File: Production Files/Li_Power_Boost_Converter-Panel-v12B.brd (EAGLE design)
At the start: 121.9 x 118.9 mm, 643 parts, among them U1 TPS61200, U10 TPS61200, U11 TPS61200, U12 TPS61200, U13 TPS61200, U14 TPS61200, U15 TPS61200, U16 TPS61200, U17 TPS61200, U18 TPS61200, U19 TPS61200, U2 TPS61200, U20 TPS61200, U21 TPS61200, U22 TPS61200, U23 TPS61200, U24 TPS61200, U25 TPS61200, U26 TPS61200, U27 TPS61200, U28 TPS61200, U29 TPS61200, U3 TPS61200, U30 TPS61200, U31 TPS61200, U32 TPS61200, U4 TPS61200, U5 TPS61200, U6 TPS61200, U7 TPS61200, U8 TPS61200, U9 TPS61200

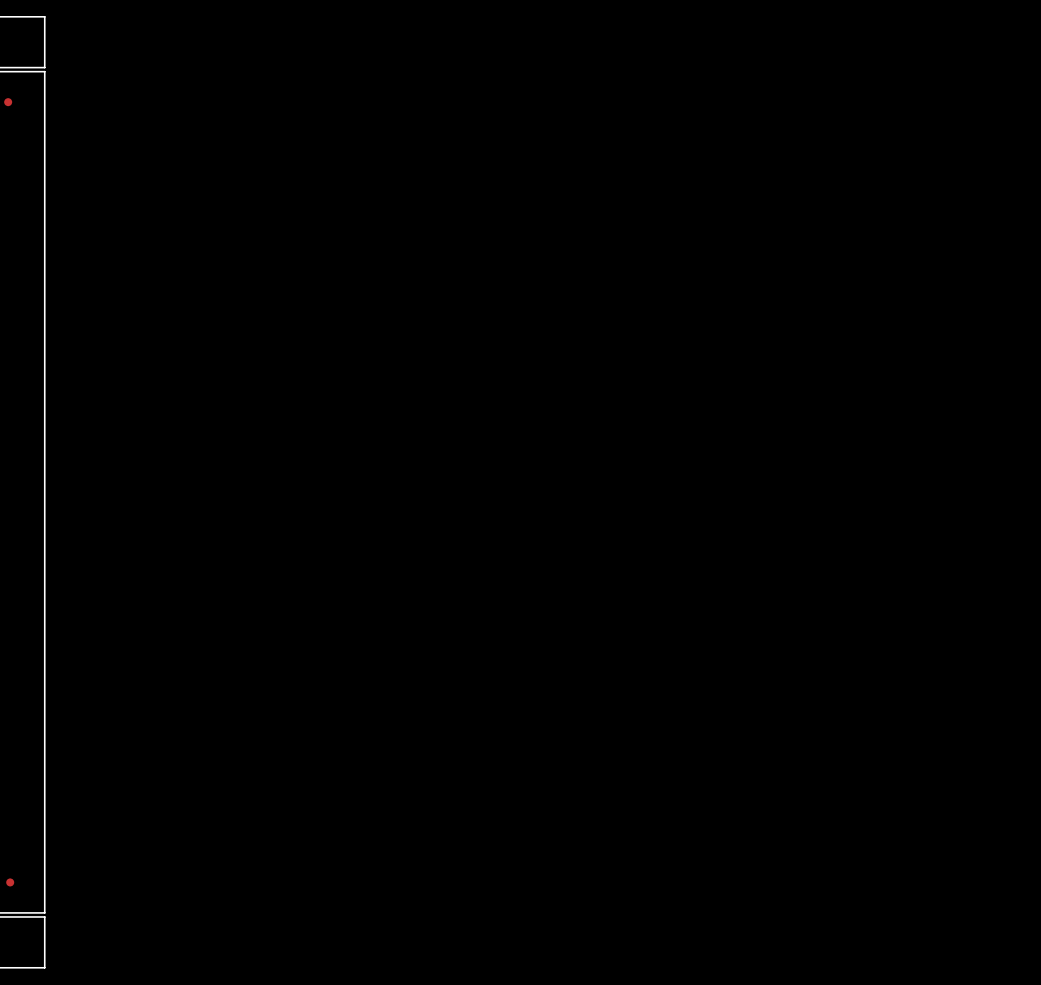
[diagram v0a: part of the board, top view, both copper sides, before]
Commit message: Repanel Production files
doubled panel size to optimize for foil use.
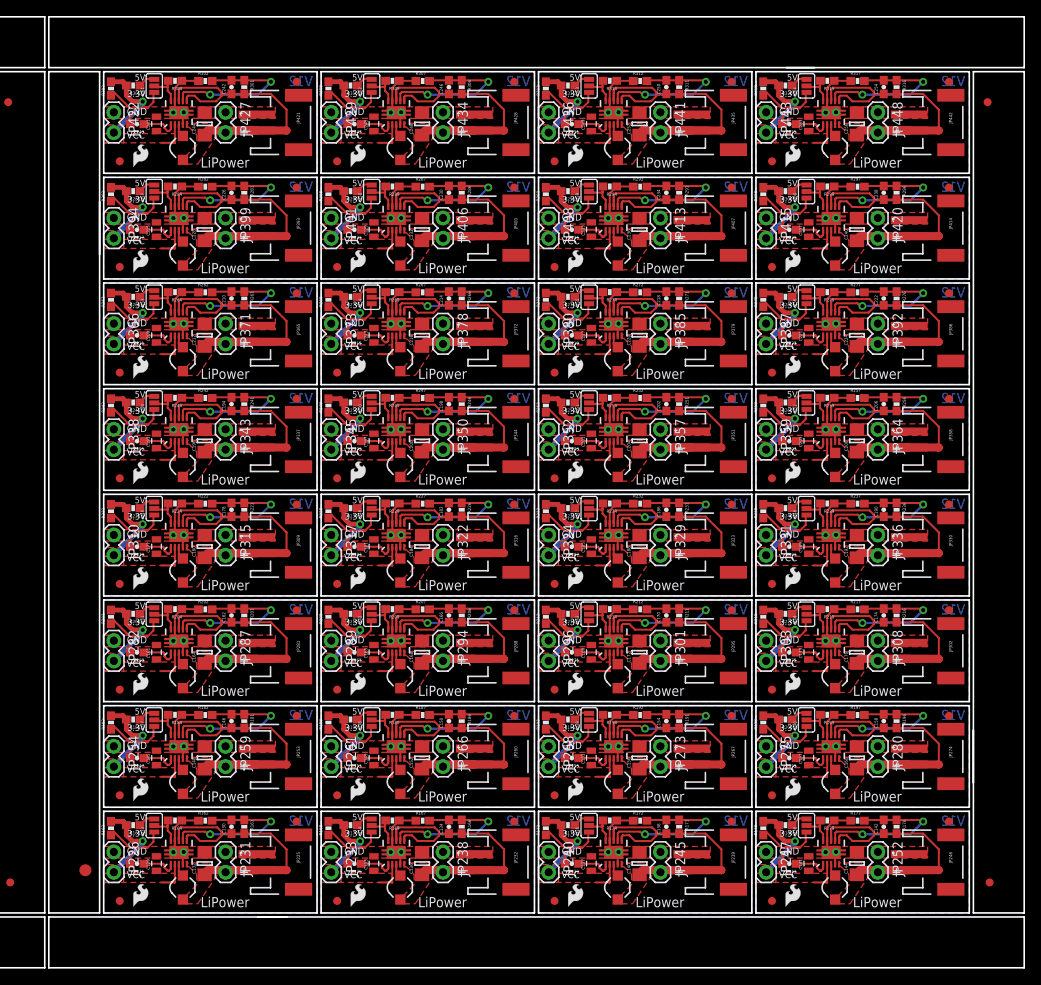
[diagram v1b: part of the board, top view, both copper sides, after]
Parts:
- added C129, C133, C137, C141, C145, C149, C153, C157, C161, C165, C169, C173, C177, C181, C185, C189, C193, C197, C201, C205, C209, C213, C217, C221, C225, C229, C233, C237, C241, C245, C249, C253: 22uF, CH_passive:0805
- added C130, C131, C134, C135, C138, C139, C142, C143, C146, C147, C150, C151, C154, C155, C158, C159, C162, C163, C166, C167, C170, C171, C174, C175, C178, C179, C182, C183, C186, C187, C190, C191, C194, C195, C198, C199, C202, C203, C206, C207, C210, C211, C214, C215, C218, C219, C222, C223, C226, C227, C230, C231, C234, C235, C238, C239, C242, C243, C246, C247, C250, C251, C254, C255: 0.1uF, SparkFun:0603-CAP
- added C132, C136, C140, C144, C148, C152, C156, C160, C164, C168, C172, C176, C180, C184, C188, C192, C196, C200, C204, C208, C212, C216, C220, C224, C228, C232, C236, C240, C244, C248, C252, C256: 10uF, CH_passive:1206
- added E$2, E$3: (no value), SparkFun-Aesthetics:FIDUCIAL-1X2
- added E$6: (no value), SparkFun-Aesthetics:FIDUCIAL-1.5X3
- added JP225, JP232, JP239, JP246, JP253, JP260, JP267, JP274, JP281, JP288, JP295, JP302, JP309, JP316, JP323, JP330, JP337, JP344, JP351, JP358, JP365, JP372, JP379, JP386, JP393, JP400, JP407, JP414, JP421, JP428, JP435, JP442: JST, SparkFun:JST-2-SMD
- added JP226, JP233, JP240, JP247, JP254, JP261, JP268, JP275, JP282, JP289, JP296, JP303, JP310, JP317, JP324, JP331, JP338, JP345, JP352, JP359, JP366, JP373, JP380, JP387, JP394, JP401, JP408, JP415, JP422, JP429, JP436, JP443: VOUT, SparkFun:1X02
- added JP227, JP234, JP241, JP248, JP255, JP262, JP269, JP276, JP283, JP290, JP297, JP304, JP311, JP318, JP325, JP332, JP339, JP346, JP353, JP360, JP367, JP374, JP381, JP388, JP395, JP402, JP409, JP416, JP423, JP430, JP437, JP444: LOGO-SFESK, SparkFun:SFE-LOGO-FLAME
- added JP228, JP229, JP235, JP236, JP242, JP243, JP249, JP250, JP256, JP257, JP263, JP264, JP270, JP271, JP277, JP278, JP284, JP285, JP291, JP292, JP298, JP299, JP305, JP306, JP312, JP313, JP319, JP320, JP326, JP327, JP333, JP334, JP340, JP341, JP347, JP348, JP354, JP355, JP361, JP362, JP368, JP369, JP375, JP376, JP382, JP383, JP389, JP390, JP396, JP397, JP403, JP404, JP410, JP411, JP417, JP418, JP424, JP425, JP431, JP432, JP438, JP439, JP445, JP446: FIDUCIAL1X2, SparkFun:FIDUCIAL-1X2
- added JP230, JP237, JP244, JP251, JP258, JP265, JP272, JP279, JP286, JP293, JP300, JP307, JP314, JP321, JP328, JP335, JP342, JP349, JP356, JP363, JP370, JP377, JP384, JP391, JP398, JP405, JP412, JP419, JP426, JP433, JP440, JP447: LOGO-SFENEW, SparkFun:SFE-NEW-WEBLOGO
- added JP231, JP238, JP245, JP252, JP259, JP266, JP273, JP280, JP287, JP294, JP301, JP308, JP315, JP322, JP329, JP336, JP343, JP350, JP357, JP364, JP371, JP378, JP385, JP392, JP399, JP406, JP413, JP420, JP427, JP434, JP441, JP448: VIN, SparkFun:1X02
- added L33, L34, L35, L36, L37, L38, L39, L40, L41, L42, L43, L44, L45, L46, L47, L48, L49, L50, L51, L52, L53, L54, L55, L56, L57, L58, L59, L60, L61, L62, L63, L64: 4.7uH, 1.2A, SparkFun:CDRH2D09
- added R161, R165, R166, R170, R171, R175, R176, R180, R181, R185, R186, R190, R191, R195, R196, R200, R201, R205, R206, R210, R211, R215, R216, R220, R221, R225, R226, R230, R231, R235, R236, R240, R241, R245, R246, R250, R251, R255, R256, R260, R261, R265, R266, R270, R271, R275, R276, R280, R281, R285, R286, R290, R291, R295, R296, R300, R301, R305, R306, R310, R311, R315, R316, R320: 2M, SparkFun:0603-RES
- added R162, R164, R167, R169, R172, R174, R177, R179, R182, R184, R187, R189, R192, R194, R197, R199, R202, R204, R207, R209, R212, R214, R217, R219, R222, R224, R227, R229, R232, R234, R237, R239, R242, R244, R247, R249, R252, R254, R257, R259, R262, R264, R267, R269, R272, R274, R277, R279, R282, R284, R287, R289, R292, R294, R297, R299, R302, R304, R307, R309, R312, R314, R317, R319: 220k, SparkFun:0603-RES
- added R163, R168, R173, R178, R183, R188, R193, R198, R203, R208, R213, R218, R223, R228, R233, R238, R243, R248, R253, R258, R263, R268, R273, R278, R283, R288, R293, R298, R303, R308, R313, R318: 1.2M, SparkFun:0603-RES
- added SJ33, SJ34, SJ35, SJ36, SJ37, SJ38, SJ39, SJ40, SJ41, SJ42, SJ43, SJ44, SJ45, SJ46, SJ47, SJ48, SJ49, SJ50, SJ51, SJ52, SJ53, SJ54, SJ55, SJ56, SJ57, SJ58, SJ59, SJ60, SJ61, SJ62, SJ63, SJ64: (no value), SparkFun:SJ_3_PASTE2&3
- added U$33, U$34, U$35, U$36, U$37, U$38, U$39, U$40, U$41, U$42, U$43, U$44, U$45, U$46, U$47, U$48, U$49, U$50, U$51, U$52, U$53, U$54, U$55, U$56, U$57, U$58, U$59, U$60, U$61, U$62, U$63, U$64: (no value), SparkFun-Aesthetics:OSHW-LOGO-S
- added U33, U34, U35, U36, U37, U38, U39, U40, U41, U42, U43, U44, U45, U46, U47, U48, U49, U50, U51, U52, U53, U54, U55, U56, U57, U58, U59, U60, U61, U62, U63, U64: TPS61200, SparkFun:QFN-10_PAD
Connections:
- new net 3.3V32: R163.1, SJ33.1
- new net 3.3V33: R168.1, SJ34.1
- new net 3.3V34: R173.1, SJ35.1
- new net 3.3V35: R178.1, SJ36.1
- new net 3.3V36: R183.1, SJ37.1
- new net 3.3V37: R188.1, SJ38.1
- new net 3.3V38: R193.1, SJ39.1
- new net 3.3V39: R198.1, SJ40.1
- new net 3.3V40: R203.1, SJ41.1
- new net 3.3V41: R208.1, SJ42.1
- new net 3.3V42: R213.1, SJ43.1
- new net 3.3V43: R218.1, SJ44.1
- new net 3.3V44: R223.1, SJ45.1
- new net 3.3V45: R228.1, SJ46.1
- new net 3.3V46: R233.1, SJ47.1
- new net 3.3V47: R238.1, SJ48.1
- new net 3.3V48: R243.1, SJ49.1
- new net 3.3V49: R248.1, SJ50.1
- new net 3.3V50: R253.1, SJ51.1
- new net 3.3V51: R258.1, SJ52.1
- new net 3.3V52: R263.1, SJ53.1
- new net 3.3V53: R268.1, SJ54.1
- new net 3.3V54: R273.1, SJ55.1
- new net 3.3V55: R278.1, SJ56.1
- new net 3.3V56: R283.1, SJ57.1
- new net 3.3V57: R288.1, SJ58.1
- new net 3.3V58: R293.1, SJ59.1
- new net 3.3V59: R298.1, SJ60.1
- new net 3.3V60: R303.1, SJ61.1
- new net 3.3V61: R308.1, SJ62.1
- new net 3.3V62: R313.1, SJ63.1
- new net 3.3V63: R318.1, SJ64.1
- new net 5V32: R165.1, SJ33.3
- new net 5V33: R170.1, SJ34.3
- new net 5V34: R175.1, SJ35.3
- new net 5V35: R180.1, SJ36.3
- new net 5V36: R185.1, SJ37.3
- new net 5V37: R190.1, SJ38.3
- new net 5V38: R195.1, SJ39.3
- new net 5V39: R200.1, SJ40.3
- new net 5V40: R205.1, SJ41.3
- new net 5V41: R210.1, SJ42.3
- new net 5V42: R215.1, SJ43.3
- new net 5V43: R220.1, SJ44.3
- new net 5V44: R225.1, SJ45.3
- new net 5V45: R230.1, SJ46.3
- new net 5V46: R235.1, SJ47.3
- new net 5V47: R240.1, SJ48.3
- new net 5V48: R245.1, SJ49.3
- new net 5V49: R250.1, SJ50.3
- new net 5V50: R255.1, SJ51.3
- new net 5V51: R260.1, SJ52.3
- new net 5V52: R265.1, SJ53.3
- new net 5V53: R270.1, SJ54.3
- new net 5V54: R275.1, SJ55.3
- new net 5V55: R280.1, SJ56.3
- new net 5V56: R285.1, SJ57.3
- new net 5V57: R290.1, SJ58.3
- new net 5V58: R295.1, SJ59.3
- new net 5V59: R300.1, SJ60.3
- new net 5V60: R305.1, SJ61.3
- new net 5V61: R310.1, SJ62.3
- new net 5V62: R315.1, SJ63.3
- new net 5V63: R320.1, SJ64.3
- new net FB32: R164.2, SJ33.2, U33.10
- new net FB33: R169.2, SJ34.2, U34.10
- new net FB34: R174.2, SJ35.2, U35.10
- new net FB35: R179.2, SJ36.2, U36.10
- new net FB36: R184.2, SJ37.2, U37.10
- new net FB37: R189.2, SJ38.2, U38.10
- new net FB38: R194.2, SJ39.2, U39.10
- new net FB39: R199.2, SJ40.2, U40.10
- new net FB40: R204.2, SJ41.2, U41.10
- new net FB41: R209.2, SJ42.2, U42.10
- new net FB42: R214.2, SJ43.2, U43.10
- new net FB43: R219.2, SJ44.2, U44.10
- new net FB44: R224.2, SJ45.2, U45.10
- new net FB45: R229.2, SJ46.2, U46.10
- new net FB46: R234.2, SJ47.2, U47.10
- new net FB47: R239.2, SJ48.2, U48.10
- new net FB48: R244.2, SJ49.2, U49.10
- new net FB49: R249.2, SJ50.2, U50.10
- new net FB50: R254.2, SJ51.2, U51.10
- new net FB51: R259.2, SJ52.2, U52.10
- new net FB52: R264.2, SJ53.2, U53.10
- new net FB53: R269.2, SJ54.2, U54.10
- new net FB54: R274.2, SJ55.2, U55.10
- new net FB55: R279.2, SJ56.2, U56.10
- new net FB56: R284.2, SJ57.2, U57.10
- new net FB57: R289.2, SJ58.2, U58.10
- new net FB58: R294.2, SJ59.2, U59.10
- new net FB59: R299.2, SJ60.2, U60.10
- new net FB60: R304.2, SJ61.2, U61.10
- new net FB61: R309.2, SJ62.2, U62.10
- new net FB62: R314.2, SJ63.2, U63.10
- new net FB63: R319.2, SJ64.2, U64.10
- new net GND32: C129.2, C131.2, C132.2, JP225.1, JP226.1, JP231.1, R162.1, R164.1, U33.11, U33.12, U33.13, U33.14, U33.15, U33.4, U33.9
- new net GND33: C133.2, C135.2, C136.2, JP232.1, JP233.1, JP238.1, R167.1, R169.1, U34.11, U34.12, U34.13, U34.14, U34.15, U34.4, U34.9
- new net GND34: C137.2, C139.2, C140.2, JP239.1, JP240.1, JP245.1, R172.1, R174.1, U35.11, U35.12, U35.13, U35.14, U35.15, U35.4, U35.9
- new net GND35: C141.2, C143.2, C144.2, JP246.1, JP247.1, JP252.1, R177.1, R179.1, U36.11, U36.12, U36.13, U36.14, U36.15, U36.4, U36.9
- new net GND36: C145.2, C147.2, C148.2, JP253.1, JP254.1, JP259.1, R182.1, R184.1, U37.11, U37.12, U37.13, U37.14, U37.15, U37.4, U37.9
- new net GND37: C149.2, C151.2, C152.2, JP260.1, JP261.1, JP266.1, R187.1, R189.1, U38.11, U38.12, U38.13, U38.14, U38.15, U38.4, U38.9
- new net GND38: C153.2, C155.2, C156.2, JP267.1, JP268.1, JP273.1, R192.1, R194.1, U39.11, U39.12, U39.13, U39.14, U39.15, U39.4, U39.9
- new net GND39: C157.2, C159.2, C160.2, JP274.1, JP275.1, JP280.1, R197.1, R199.1, U40.11, U40.12, U40.13, U40.14, U40.15, U40.4, U40.9
- new net GND40: C161.2, C163.2, C164.2, JP281.1, JP282.1, JP287.1, R202.1, R204.1, U41.11, U41.12, U41.13, U41.14, U41.15, U41.4, U41.9
- new net GND41: C165.2, C167.2, C168.2, JP288.1, JP289.1, JP294.1, R207.1, R209.1, U42.11, U42.12, U42.13, U42.14, U42.15, U42.4, U42.9
- new net GND42: C169.2, C171.2, C172.2, JP295.1, JP296.1, JP301.1, R212.1, R214.1, U43.11, U43.12, U43.13, U43.14, U43.15, U43.4, U43.9
- new net GND43: C173.2, C175.2, C176.2, JP302.1, JP303.1, JP308.1, R217.1, R219.1, U44.11, U44.12, U44.13, U44.14, U44.15, U44.4, U44.9
- new net GND44: C177.2, C179.2, C180.2, JP309.1, JP310.1, JP315.1, R222.1, R224.1, U45.11, U45.12, U45.13, U45.14, U45.15, U45.4, U45.9
- new net GND45: C181.2, C183.2, C184.2, JP316.1, JP317.1, JP322.1, R227.1, R229.1, U46.11, U46.12, U46.13, U46.14, U46.15, U46.4, U46.9
- new net GND46: C185.2, C187.2, C188.2, JP323.1, JP324.1, JP329.1, R232.1, R234.1, U47.11, U47.12, U47.13, U47.14, U47.15, U47.4, U47.9
- new net GND47: C189.2, C191.2, C192.2, JP330.1, JP331.1, JP336.1, R237.1, R239.1, U48.11, U48.12, U48.13, U48.14, U48.15, U48.4, U48.9
- new net GND48: C193.2, C195.2, C196.2, JP337.1, JP338.1, JP343.1, R242.1, R244.1, U49.11, U49.12, U49.13, U49.14, U49.15, U49.4, U49.9
- new net GND49: C197.2, C199.2, C200.2, JP344.1, JP345.1, JP350.1, R247.1, R249.1, U50.11, U50.12, U50.13, U50.14, U50.15, U50.4, U50.9
- new net GND50: C201.2, C203.2, C204.2, JP351.1, JP352.1, JP357.1, R252.1, R254.1, U51.11, U51.12, U51.13, U51.14, U51.15, U51.4, U51.9
- new net GND51: C205.2, C207.2, C208.2, JP358.1, JP359.1, JP364.1, R257.1, R259.1, U52.11, U52.12, U52.13, U52.14, U52.15, U52.4, U52.9
- new net GND52: C209.2, C211.2, C212.2, JP365.1, JP366.1, JP371.1, R262.1, R264.1, U53.11, U53.12, U53.13, U53.14, U53.15, U53.4, U53.9
- new net GND53: C213.2, C215.2, C216.2, JP372.1, JP373.1, JP378.1, R267.1, R269.1, U54.11, U54.12, U54.13, U54.14, U54.15, U54.4, U54.9
- new net GND54: C217.2, C219.2, C220.2, JP379.1, JP380.1, JP385.1, R272.1, R274.1, U55.11, U55.12, U55.13, U55.14, U55.15, U55.4, U55.9
- new net GND55: C221.2, C223.2, C224.2, JP386.1, JP387.1, JP392.1, R277.1, R279.1, U56.11, U56.12, U56.13, U56.14, U56.15, U56.4, U56.9
- new net GND56: C225.2, C227.2, C228.2, JP393.1, JP394.1, JP399.1, R282.1, R284.1, U57.11, U57.12, U57.13, U57.14, U57.15, U57.4, U57.9
- new net GND57: C229.2, C231.2, C232.2, JP400.1, JP401.1, JP406.1, R287.1, R289.1, U58.11, U58.12, U58.13, U58.14, U58.15, U58.4, U58.9
- new net GND58: C233.2, C235.2, C236.2, JP407.1, JP408.1, JP413.1, R292.1, R294.1, U59.11, U59.12, U59.13, U59.14, U59.15, U59.4, U59.9
- new net GND59: C237.2, C239.2, C240.2, JP414.1, JP415.1, JP420.1, R297.1, R299.1, U60.11, U60.12, U60.13, U60.14, U60.15, U60.4, U60.9
- new net GND60: C241.2, C243.2, C244.2, JP421.1, JP422.1, JP427.1, R302.1, R304.1, U61.11, U61.12, U61.13, U61.14, U61.15, U61.4, U61.9
- new net GND61: C245.2, C247.2, C248.2, JP428.1, JP429.1, JP434.1, R307.1, R309.1, U62.11, U62.12, U62.13, U62.14, U62.15, U62.4, U62.9
- new net GND62: C249.2, C251.2, C252.2, JP435.1, JP436.1, JP441.1, R312.1, R314.1, U63.11, U63.12, U63.13, U63.14, U63.15, U63.4, U63.9
- new net GND63: C253.2, C255.2, C256.2, JP442.1, JP443.1, JP448.1, R317.1, R319.1, U64.11, U64.12, U64.13, U64.14, U64.15, U64.4, U64.9
- new net N$100: C199.1, U50.1
- new net N$101: L51.P$1, U51.3
- new net N$102: C203.1, U51.1
- new net N$103: L52.P$1, U52.3
- new net N$104: C207.1, U52.1
- new net N$105: L53.P$1, U53.3
- new net N$106: C211.1, U53.1
- new net N$107: L54.P$1, U54.3
- new net N$108: C215.1, U54.1
- new net N$109: L55.P$1, U55.3
- new net N$110: C219.1, U55.1
- new net N$111: L56.P$1, U56.3
- new net N$112: C223.1, U56.1
- new net N$113: L57.P$1, U57.3
- new net N$114: C227.1, U57.1
- new net N$115: L58.P$1, U58.3
- new net N$116: C231.1, U58.1
- new net N$117: L59.P$1, U59.3
- new net N$118: C235.1, U59.1
- new net N$119: L60.P$1, U60.3
- new net N$120: C239.1, U60.1
- new net N$121: L61.P$1, U61.3
- new net N$122: C243.1, U61.1
- new net N$123: L62.P$1, U62.3
- new net N$124: C247.1, U62.1
- new net N$125: L63.P$1, U63.3
- new net N$126: C251.1, U63.1
- new net N$127: L64.P$1, U64.3
- new net N$128: C255.1, U64.1
- new net N$65: L33.P$1, U33.3
- new net N$66: C131.1, U33.1
- new net N$67: L34.P$1, U34.3
- new net N$68: C135.1, U34.1
- new net N$69: L35.P$1, U35.3
- new net N$70: C139.1, U35.1
- new net N$71: L36.P$1, U36.3
- new net N$72: C143.1, U36.1
- new net N$73: L37.P$1, U37.3
- new net N$74: C147.1, U37.1
- new net N$75: L38.P$1, U38.3
- new net N$76: C151.1, U38.1
- new net N$77: L39.P$1, U39.3
- new net N$78: C155.1, U39.1
- new net N$79: L40.P$1, U40.3
- new net N$80: C159.1, U40.1
- new net N$81: L41.P$1, U41.3
- new net N$82: C163.1, U41.1
- new net N$83: L42.P$1, U42.3
- new net N$84: C167.1, U42.1
- new net N$85: L43.P$1, U43.3
- new net N$86: C171.1, U43.1
- new net N$87: L44.P$1, U44.3
- new net N$88: C175.1, U44.1
- new net N$89: L45.P$1, U45.3
- new net N$90: C179.1, U45.1
- new net N$91: L46.P$1, U46.3
- new net N$92: C183.1, U46.1
- new net N$93: L47.P$1, U47.3
- new net N$94: C187.1, U47.1
- new net N$95: L48.P$1, U48.3
- new net N$96: C191.1, U48.1
- new net N$97: L49.P$1, U49.3
- new net N$98: C195.1, U49.1
- new net N$99: L50.P$1, U50.3
- new net UVLO32: C130.2, R161.1, R162.2, U33.7
- new net UVLO33: C134.2, R166.1, R167.2, U34.7
- new net UVLO34: C138.2, R171.1, R172.2, U35.7
- new net UVLO35: C142.2, R176.1, R177.2, U36.7
- new net UVLO36: C146.2, R181.1, R182.2, U37.7
- new net UVLO37: C150.2, R186.1, R187.2, U38.7
- new net UVLO38: C154.2, R191.1, R192.2, U39.7
- new net UVLO39: C158.2, R196.1, R197.2, U40.7
- new net UVLO40: C162.2, R201.1, R202.2, U41.7
- new net UVLO41: C166.2, R206.1, R207.2, U42.7
- new net UVLO42: C170.2, R211.1, R212.2, U43.7
- new net UVLO43: C174.2, R216.1, R217.2, U44.7
- new net UVLO44: C178.2, R221.1, R222.2, U45.7
- new net UVLO45: C182.2, R226.1, R227.2, U46.7
- new net UVLO46: C186.2, R231.1, R232.2, U47.7
- new net UVLO47: C190.2, R236.1, R237.2, U48.7
- new net UVLO48: C194.2, R241.1, R242.2, U49.7
- new net UVLO49: C198.2, R246.1, R247.2, U50.7
- new net UVLO50: C202.2, R251.1, R252.2, U51.7
- new net UVLO51: C206.2, R256.1, R257.2, U52.7
- new net UVLO52: C210.2, R261.1, R262.2, U53.7
- new net UVLO53: C214.2, R266.1, R267.2, U54.7
- new net UVLO54: C218.2, R271.1, R272.2, U55.7
- new net UVLO55: C222.2, R276.1, R277.2, U56.7
- new net UVLO56: C226.2, R281.1, R282.2, U57.7
- new net UVLO57: C230.2, R286.1, R287.2, U58.7
- new net UVLO58: C234.2, R291.1, R292.2, U59.7
- new net UVLO59: C238.2, R296.1, R297.2, U60.7
- new net UVLO60: C242.2, R301.1, R302.2, U61.7
- new net UVLO61: C246.2, R306.1, R307.2, U62.7
- new net UVLO62: C250.2, R311.1, R312.2, U63.7
- new net UVLO63: C254.2, R316.1, R317.2, U64.7
- new net VCC32: C129.1, JP226.2, R163.2, R165.2, U33.2
- new net VCC33: C133.1, JP233.2, R168.2, R170.2, U34.2
- new net VCC34: C137.1, JP240.2, R173.2, R175.2, U35.2
- new net VCC35: C141.1, JP247.2, R178.2, R180.2, U36.2
- new net VCC36: C145.1, JP254.2, R183.2, R185.2, U37.2
- new net VCC37: C149.1, JP261.2, R188.2, R190.2, U38.2
- new net VCC38: C153.1, JP268.2, R193.2, R195.2, U39.2
- new net VCC39: C157.1, JP275.2, R198.2, R200.2, U40.2
- new net VCC40: C161.1, JP282.2, R203.2, R205.2, U41.2
- new net VCC41: C165.1, JP289.2, R208.2, R210.2, U42.2
- new net VCC42: C169.1, JP296.2, R213.2, R215.2, U43.2
- new net VCC43: C173.1, JP303.2, R218.2, R220.2, U44.2
- new net VCC44: C177.1, JP310.2, R223.2, R225.2, U45.2
- new net VCC45: C181.1, JP317.2, R228.2, R230.2, U46.2
- new net VCC46: C185.1, JP324.2, R233.2, R235.2, U47.2
- new net VCC47: C189.1, JP331.2, R238.2, R240.2, U48.2
- new net VCC48: C193.1, JP338.2, R243.2, R245.2, U49.2
- new net VCC49: C197.1, JP345.2, R248.2, R250.2, U50.2
- new net VCC50: C201.1, JP352.2, R253.2, R255.2, U51.2
- new net VCC51: C205.1, JP359.2, R258.2, R260.2, U52.2
- new net VCC52: C209.1, JP366.2, R263.2, R265.2, U53.2
- new net VCC53: C213.1, JP373.2, R268.2, R270.2, U54.2
- new net VCC54: C217.1, JP380.2, R273.2, R275.2, U55.2
- new net VCC55: C221.1, JP387.2, R278.2, R280.2, U56.2
- new net VCC56: C225.1, JP394.2, R283.2, R285.2, U57.2
- new net VCC57: C229.1, JP401.2, R288.2, R290.2, U58.2
- new net VCC58: C233.1, JP408.2, R293.2, R295.2, U59.2
- new net VCC59: C237.1, JP415.2, R298.2, R300.2, U60.2
- new net VCC60: C241.1, JP422.2, R303.2, R305.2, U61.2
- new net VCC61: C245.1, JP429.2, R308.2, R310.2, U62.2
- new net VCC62: C249.1, JP436.2, R313.2, R315.2, U63.2
- new net VCC63: C253.1, JP443.2, R318.2, R320.2, U64.2
- new net VIN32: C130.1, C132.1, JP225.2, JP231.2, L33.P$2, R161.2, U33.5, U33.6, U33.8
- new net VIN33: C134.1, C136.1, JP232.2, JP238.2, L34.P$2, R166.2, U34.5, U34.6, U34.8
- new net VIN34: C138.1, C140.1, JP239.2, JP245.2, L35.P$2, R171.2, U35.5, U35.6, U35.8
- new net VIN35: C142.1, C144.1, JP246.2, JP252.2, L36.P$2, R176.2, U36.5, U36.6, U36.8
- new net VIN36: C146.1, C148.1, JP253.2, JP259.2, L37.P$2, R181.2, U37.5, U37.6, U37.8
- new net VIN37: C150.1, C152.1, JP260.2, JP266.2, L38.P$2, R186.2, U38.5, U38.6, U38.8
- new net VIN38: C154.1, C156.1, JP267.2, JP273.2, L39.P$2, R191.2, U39.5, U39.6, U39.8
- new net VIN39: C158.1, C160.1, JP274.2, JP280.2, L40.P$2, R196.2, U40.5, U40.6, U40.8
- new net VIN40: C162.1, C164.1, JP281.2, JP287.2, L41.P$2, R201.2, U41.5, U41.6, U41.8
- new net VIN41: C166.1, C168.1, JP288.2, JP294.2, L42.P$2, R206.2, U42.5, U42.6, U42.8
- new net VIN42: C170.1, C172.1, JP295.2, JP301.2, L43.P$2, R211.2, U43.5, U43.6, U43.8
- new net VIN43: C174.1, C176.1, JP302.2, JP308.2, L44.P$2, R216.2, U44.5, U44.6, U44.8
- new net VIN44: C178.1, C180.1, JP309.2, JP315.2, L45.P$2, R221.2, U45.5, U45.6, U45.8
- new net VIN45: C182.1, C184.1, JP316.2, JP322.2, L46.P$2, R226.2, U46.5, U46.6, U46.8
- new net VIN46: C186.1, C188.1, JP323.2, JP329.2, L47.P$2, R231.2, U47.5, U47.6, U47.8
- new net VIN47: C190.1, C192.1, JP330.2, JP336.2, L48.P$2, R236.2, U48.5, U48.6, U48.8
- new net VIN48: C194.1, C196.1, JP337.2, JP343.2, L49.P$2, R241.2, U49.5, U49.6, U49.8
- new net VIN49: C198.1, C200.1, JP344.2, JP350.2, L50.P$2, R246.2, U50.5, U50.6, U50.8
- new net VIN50: C202.1, C204.1, JP351.2, JP357.2, L51.P$2, R251.2, U51.5, U51.6, U51.8
- new net VIN51: C206.1, C208.1, JP358.2, JP364.2, L52.P$2, R256.2, U52.5, U52.6, U52.8
- new net VIN52: C210.1, C212.1, JP365.2, JP371.2, L53.P$2, R261.2, U53.5, U53.6, U53.8
- new net VIN53: C214.1, C216.1, JP372.2, JP378.2, L54.P$2, R266.2, U54.5, U54.6, U54.8
- new net VIN54: C218.1, C220.1, JP379.2, JP385.2, L55.P$2, R271.2, U55.5, U55.6, U55.8
- new net VIN55: C222.1, C224.1, JP386.2, JP392.2, L56.P$2, R276.2, U56.5, U56.6, U56.8
- new net VIN56: C226.1, C228.1, JP393.2, JP399.2, L57.P$2, R281.2, U57.5, U57.6, U57.8
- new net VIN57: C230.1, C232.1, JP400.2, JP406.2, L58.P$2, R286.2, U58.5, U58.6, U58.8
- new net VIN58: C234.1, C236.1, JP407.2, JP413.2, L59.P$2, R291.2, U59.5, U59.6, U59.8
- new net VIN59: C238.1, C240.1, JP414.2, JP420.2, L60.P$2, R296.2, U60.5, U60.6, U60.8
- new net VIN60: C242.1, C244.1, JP421.2, JP427.2, L61.P$2, R301.2, U61.5, U61.6, U61.8
- new net VIN61: C246.1, C248.1, JP428.2, JP434.2, L62.P$2, R306.2, U62.5, U62.6, U62.8
- new net VIN62: C250.1, C252.1, JP435.2, JP441.2, L63.P$2, R311.2, U63.5, U63.6, U63.8
- new net VIN63: C254.1, C256.1, JP442.2, JP448.2, L64.P$2, R316.2, U64.5, U64.6, U64.8
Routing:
- net VIN56: track 0.00 -> 40.3 mm
- net VIN48: track 0.00 -> 40.3 mm
- net VIN52: track 0.00 -> 40.3 mm
- net VIN58: track 0.00 -> 40.3 mm
- net VIN57: track 0.00 -> 40.3 mm
- net VIN50: track 0.00 -> 40.3 mm
- net VIN49: track 0.00 -> 40.3 mm
- net VIN54: track 0.00 -> 40.3 mm
- net VIN53: track 0.00 -> 40.3 mm
- net VIN32: track 0.00 -> 40.3 mm
- net VIN59: track 0.00 -> 40.3 mm
- net VIN51: track 0.00 -> 40.3 mm
- net VIN44: track 0.00 -> 40.3 mm
- net VIN40: track 0.00 -> 40.3 mm
- net VIN36: track 0.00 -> 40.3 mm
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- added copper zone on layer 1, net GND32
- added copper zone on layer 16, net GND32
- added copper zone on layer 1, net GND33
- added copper zone on layer 16, net GND33
- added copper zone on layer 1, net GND34
- added copper zone on layer 16, net GND34
- added copper zone on layer 1, net GND35
- added copper zone on layer 16, net GND35
- added copper zone on layer 1, net GND36
- added copper zone on layer 16, net GND36
- added copper zone on layer 1, net GND37
- added copper zone on layer 16, net GND37
- added copper zone on layer 1, net GND38
- added copper zone on layer 16, net GND38
- added copper zone on layer 1, net GND39
- added copper zone on layer 16, net GND39
- added copper zone on layer 1, net GND40
- added copper zone on layer 16, net GND40
- added copper zone on layer 1, net GND41
- added copper zone on layer 16, net GND41
- added copper zone on layer 1, net GND42
- added copper zone on layer 16, net GND42
- added copper zone on layer 1, net GND43
- added copper zone on layer 16, net GND43
- added copper zone on layer 1, net GND44
- added copper zone on layer 16, net GND44
- added copper zone on layer 1, net GND45
- added copper zone on layer 16, net GND45
- added copper zone on layer 1, net GND46
- added copper zone on layer 16, net GND46
- added copper zone on layer 1, net GND47
- added copper zone on layer 16, net GND47
- added copper zone on layer 1, net GND48
- added copper zone on layer 16, net GND48
- added copper zone on layer 1, net GND49
- added copper zone on layer 16, net GND49
- added copper zone on layer 1, net GND50
- added copper zone on layer 16, net GND50
- added copper zone on layer 1, net GND51
- added copper zone on layer 16, net GND51
- added copper zone on layer 1, net GND52
- added copper zone on layer 16, net GND52
- added copper zone on layer 1, net GND53
- added copper zone on layer 16, net GND53
- added copper zone on layer 1, net GND54
- added copper zone on layer 16, net GND54
- added copper zone on layer 1, net GND55
- added copper zone on layer 16, net GND55
- added copper zone on layer 1, net GND56
- added copper zone on layer 16, net GND56
- added copper zone on layer 1, net GND57
- added copper zone on layer 16, net GND57
- added copper zone on layer 1, net GND58
- added copper zone on layer 16, net GND58
- added copper zone on layer 1, net GND59
- added copper zone on layer 16, net GND59
- added copper zone on layer 1, net GND60
- added copper zone on layer 16, net GND60
- added copper zone on layer 1, net GND61
- added copper zone on layer 16, net GND61
- added copper zone on layer 1, net GND62
- added copper zone on layer 16, net GND62
- added copper zone on layer 1, net GND63
- added copper zone on layer 16, net GND63
- added copper zone on layer 1, net VCC32
- added copper zone on layer 1, net VCC33
- added copper zone on layer 1, net VCC34
- added copper zone on layer 1, net VCC35
- added copper zone on layer 1, net VCC36
- added copper zone on layer 1, net VCC37
- added copper zone on layer 1, net VCC38
- added copper zone on layer 1, net VCC39
- added copper zone on layer 1, net VCC40
- added copper zone on layer 1, net VCC41
- added copper zone on layer 1, net VCC42
- added copper zone on layer 1, net VCC43
- added copper zone on layer 1, net VCC44
- added copper zone on layer 1, net VCC45
- added copper zone on layer 1, net VCC46
- added copper zone on layer 1, net VCC47
- added copper zone on layer 1, net VCC48
- added copper zone on layer 1, net VCC49
- added copper zone on layer 1, net VCC50
- added copper zone on layer 1, net VCC51
- added copper zone on layer 1, net VCC52
- added copper zone on layer 1, net VCC53
- added copper zone on layer 1, net VCC54
- added copper zone on layer 1, net VCC55
- added copper zone on layer 1, net VCC56
- added copper zone on layer 1, net VCC57
- added copper zone on layer 1, net VCC58
- added copper zone on layer 1, net VCC59
- added copper zone on layer 1, net VCC60
- added copper zone on layer 1, net VCC61
- added copper zone on layer 1, net VCC62
- added copper zone on layer 1, net VCC63
- added copper zone on layer 1, net VIN32
- added copper zone on layer 1, net VIN33
- added copper zone on layer 1, net VIN34
- added copper zone on layer 1, net VIN35
- added copper zone on layer 1, net VIN36
- added copper zone on layer 1, net VIN37
- added copper zone on layer 1, net VIN38
- added copper zone on layer 1, net VIN39
- added copper zone on layer 1, net VIN40
- added copper zone on layer 1, net VIN41
- added copper zone on layer 1, net VIN42
- added copper zone on layer 1, net VIN43
- added copper zone on layer 1, net VIN44
- added copper zone on layer 1, net VIN45
- added copper zone on layer 1, net VIN46
- added copper zone on layer 1, net VIN47
- added copper zone on layer 1, net VIN48
- added copper zone on layer 1, net VIN49
- added copper zone on layer 1, net VIN50
- added copper zone on layer 1, net VIN51
- added copper zone on layer 1, net VIN52
- added copper zone on layer 1, net VIN53
- added copper zone on layer 1, net VIN54
- added copper zone on layer 1, net VIN55
- added copper zone on layer 1, net VIN56
- added copper zone on layer 1, net VIN57
- added copper zone on layer 1, net VIN58
- added copper zone on layer 1, net VIN59
- added copper zone on layer 1, net VIN60
- added copper zone on layer 1, net VIN61
- added copper zone on layer 1, net VIN62
- added copper zone on layer 1, net VIN63
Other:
- board size 121.9 x 118.9 mm -> 244.3 x 118.9 mm
